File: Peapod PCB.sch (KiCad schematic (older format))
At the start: 16 parts, among them U1 ESP8266

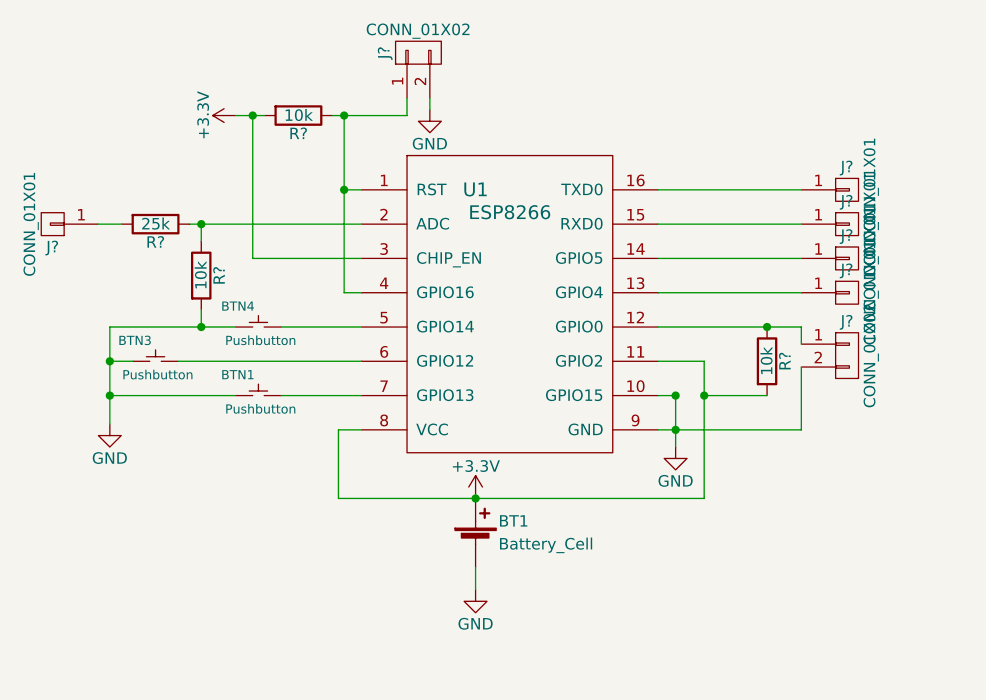
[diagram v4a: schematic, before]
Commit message: assigned footprints
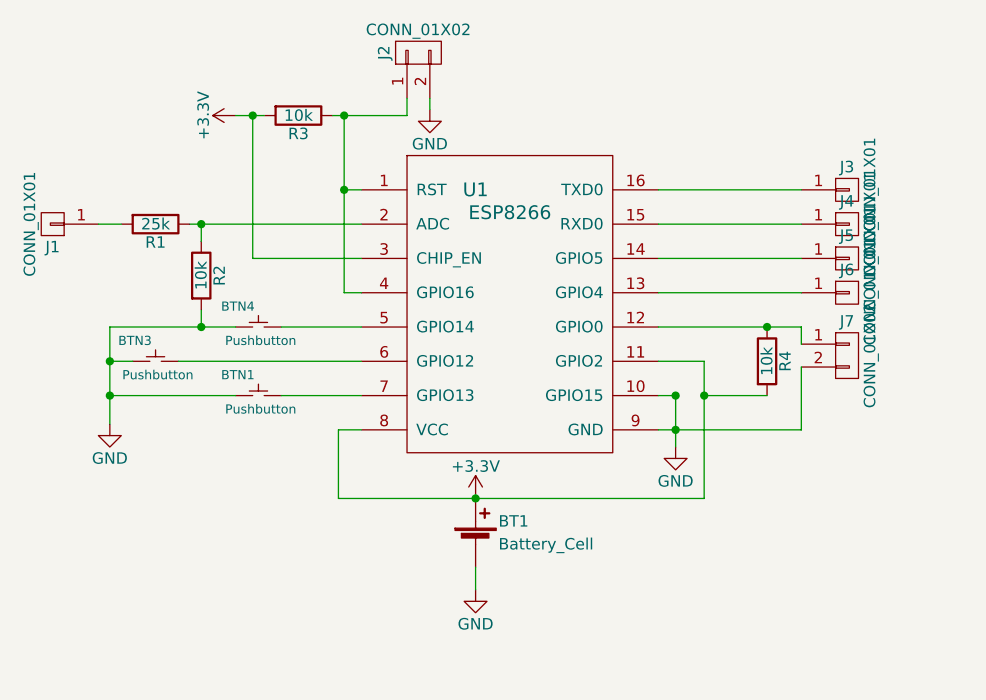
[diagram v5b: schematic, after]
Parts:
- BT1: footprint (none) -> mod:Battery Mount
- J1, J3, J4, J5, J6: renamed from J?; footprint (none) -> mod:Alligator Pad
- J2, J7: renamed from J?; footprint (none) -> mod:Bridge Pad
- R1, R2, R3, R4: renamed from R?; footprint (none) -> Resistors_SMD:R_0805_HandSoldering
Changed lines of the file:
@@
 F 0 "BT1" H 5925 4525 50  0000 L CNN
 F 1 "Battery_Cell" H 5925 4425 50  0000 L CNN
-F 2 "" V 5825 4485 50  0001 C CNN
+F 2 "mod:Battery Mount" V 5825 4485 50  0001 C CNN
 F 3 "" V 5825 4485 50  0001 C CNN
 	1    5825 4425
@@
 $EndComp
 $Comp
-L GND #PWR?
+L GND #PWR03
 U 1 1 5993357D
 P 4225 3900
-F 0 "#PWR?" H 4225 3650 50  0001 C CNN
+F 0 "#PWR03" H 4225 3650 50  0001 C CNN
 F 1 "GND" H 4225 3750 50  0000 C CNN
 F 2 "" H 4225 3900 50  0001 C CNN
@@
 $EndComp
 $Comp
-L CONN_01X01 J?
+L CONN_01X01 J3
 U 1 1 59933B2D
 P 7450 2875
-F 0 "J?" H 7450 2975 50  0000 C CNN
+F 0 "J3" H 7450 2975 50  0000 C CNN
 F 1 "CONN_01X01" V 7550 2875 50  0000 C CNN
-F 2 "" H 7450 2875 50  0001 C CNN
+F 2 "mod:Alligator Pad" H 7450 2875 50  0001 C CNN
 F 3 "" H 7450 2875 50  0001 C CNN
 	1    7450 2875
@@
 $EndComp
 $Comp
-L CONN_01X01 J?
+L CONN_01X01 J4
 U 1 1 59933BB9
 P 7450 3025
-F 0 "J?" H 7450 3125 50  0000 C CNN
+F 0 "J4" H 7450 3125 50  0000 C CNN
 F 1 "CONN_01X01" V 7550 3025 50  0000 C CNN
-F 2 "" H 7450 3025 50  0001 C CNN
+F 2 "mod:Alligator Pad" H 7450 3025 50  0001 C CNN
 F 3 "" H 7450 3025 50  0001 C CNN
 	1    7450 3025
@@
 $EndComp
 $Comp
-L CONN_01X01 J?
+L CONN_01X01 J5
 U 1 1 59933C1C
 P 7450 3175
-F 0 "J?" H 7450 3275 50  0000 C CNN
+F 0 "J5" H 7450 3275 50  0000 C CNN
 F 1 "CONN_01X01" V 7550 3175 50  0000 C CNN
-F 2 "" H 7450 3175 50  0001 C CNN
+F 2 "mod:Alligator Pad" H 7450 3175 50  0001 C CNN
 F 3 "" H 7450 3175 50  0001 C CNN
 	1    7450 3175
@@
 $EndComp
 $Comp
-L CONN_01X01 J?
+L CONN_01X01 J6
 U 1 1 59933C73
 P 7450 3325
-F 0 "J?" H 7450 3425 50  0000 C CNN
+F 0 "J6" H 7450 3425 50  0000 C CNN
 F 1 "CONN_01X01" V 7550 3325 50  0000 C CNN
-F 2 "" H 7450 3325 50  0001 C CNN
+F 2 "mod:Alligator Pad" H 7450 3325 50  0001 C CNN
 F 3 "" H 7450 3325 50  0001 C CNN
 	1    7450 3325
@@
 $EndComp
 $Comp
-L CONN_01X01 J?
+L CONN_01X01 J1
 U 1 1 59933CDE
 P 3975 3025
-F 0 "J?" H 3975 3125 50  0000 C CNN
+F 0 "J1" H 3975 3125 50  0000 C CNN
 F 1 "CONN_01X01" V 4075 3025 50  0000 C CNN
-F 2 "" H 3975 3025 50  0001 C CNN
+F 2 "mod:Alligator Pad" H 3975 3025 50  0001 C CNN
 F 3 "" H 3975 3025 50  0001 C CNN
 	1    3975 3025
@@
 $EndComp
 $Comp
-L R R?
+L R R3
 U 1 1 59933DD5
 P 5050 2550
-F 0 "R?" V 5130 2550 50  0000 C CNN
+F 0 "R3" V 5130 2550 50  0000 C CNN
 F 1 "10k" V 5050 2550 50  0000 C CNN
-F 2 "" V 4980 2550 50  0001 C CNN
+F 2 "Resistors_SMD:R_0805_HandSoldering" V 4980 2550 50  0001 C CNN
 F 3 "" H 5050 2550 50  0001 C CNN
 	1    5050 2550
@@
 $EndComp
 $Comp
-L +3.3V #PWR?
+L +3.3V #PWR04
 U 1 1 59933FE4
 P 4775 2550
-F 0 "#PWR?" H 4775 2400 50  0001 C CNN
+F 0 "#PWR04" H 4775 2400 50  0001 C CNN
 F 1 "+3.3V" H 4775 2690 50  0000 C CNN
 F 2 "" H 4775 2550 50  0001 C CNN
@@
 $EndComp
 $Comp
-L +3.3V #PWR?
+L +3.3V #PWR05
 U 1 1 59934256
 P 5825 4225
-F 0 "#PWR?" H 5825 4075 50  0001 C CNN
+F 0 "#PWR05" H 5825 4075 50  0001 C CNN
 F 1 "+3.3V" H 5825 4365 50  0000 C CNN
 F 2 "" H 5825 4225 50  0001 C CNN
@@
 $EndComp
 $Comp
-L R R?
+L R R1
 U 1 1 59934609
 P 4425 3025
-F 0 "R?" V 4505 3025 50  0000 C CNN
+F 0 "R1" V 4505 3025 50  0000 C CNN
 F 1 "25k" V 4425 3025 50  0000 C CNN
-F 2 "" V 4355 3025 50  0001 C CNN
+F 2 "Resistors_SMD:R_0805_HandSoldering" V 4355 3025 50  0001 C CNN
 F 3 "" H 4425 3025 50  0001 C CNN
 	1    4425 3025
@@
 	4275 3025 4175 3025
 $Comp
-L R R?
+L R R2
 U 1 1 59934849
 P 4625 3250
-F 0 "R?" V 4705 3250 50  0000 C CNN
+F 0 "R2" V 4705 3250 50  0000 C CNN
 F 1 "10k" V 4625 3250 50  0000 C CNN
-F 2 "" V 4555 3250 50  0001 C CNN
+F 2 "Resistors_SMD:R_0805_HandSoldering" V 4555 3250 50  0001 C CNN
 F 3 "" H 4625 3250 50  0001 C CNN
 	1    4625 3250
@@
 Connection ~ 4625 3475
 $Comp
-L CONN_01X02 J?
+L CONN_01X02 J7
 U 1 1 5993514F
 P 7450 3600
-F 0 "J?" H 7450 3750 50  0000 C CNN
+F 0 "J7" H 7450 3750 50  0000 C CNN
 F 1 "CONN_01X02" V 7550 3600 50  0000 C CNN
-F 2 "" H 7450 3600 50  0001 C CNN
+F 2 "mod:Bridge Pad" H 7450 3600 50  0001 C CNN
 F 3 "" H 7450 3600 50  0001 C CNN
 	1    7450 3600
@@
 Connection ~ 6700 3775
 $Comp
-L R R?
+L R R4
 U 1 1 59935339
 P 7100 3625
-F 0 "R?" V 7180 3625 50  0000 C CNN
+F 0 "R4" V 7180 3625 50  0000 C CNN
 F 1 "10k" V 7100 3625 50  0000 C CNN
-F 2 "" V 7030 3625 50  0001 C CNN
+F 2 "Resistors_SMD:R_0805_HandSoldering" V 7030 3625 50  0001 C CNN
 F 3 "" H 7100 3625 50  0001 C CNN
 	1    7100 3625
@@
 Connection ~ 6825 3775
 $Comp
-L CONN_01X02 J?
+L CONN_01X02 J2
 U 1 1 5993627D
 P 5575 2275
-F 0 "J?" H 5575 2425 50  0000 C CNN
+F 0 "J2" H 5575 2425 50  0000 C CNN
 F 1 "CONN_01X02" V 5675 2275 50  0000 C CNN
-F 2 "" H 5575 2275 50  0001 C CNN
+F 2 "mod:Bridge Pad" H 5575 2275 50  0001 C CNN
 F 3 "" H 5575 2275 50  0001 C CNN
 	1    5575 2275
@@
 Connection ~ 5250 2550
 $Comp
-L GND #PWR?
+L GND #PWR06
 U 1 1 599363AF
 P 5625 2525
-F 0 "#PWR?" H 5625 2275 50  0001 C CNN
+F 0 "#PWR06" H 5625 2275 50  0001 C CNN
 F 1 "GND" H 5625 2375 50  0000 C CNN
 F 2 "" H 5625 2525 50  0001 C CNN

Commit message: finished assigning footprints to components
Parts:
- BTN1, BTN3, BTN4: footprint (none) -> mod:Pushbutton
- U1: footprint (none) -> mod:ESP-12E_SMD
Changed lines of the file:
@@
 F 0 "U1" H 5825 3675 60  0000 C CNN
 F 1 "ESP8266" H 5975 3575 60  0000 C CNN
-F 2 "" H 5925 3275 60  0001 C CNN
+F 2 "mod:ESP-12E_SMD" H 5925 3275 60  0001 C CNN
 F 3 "" H 5925 3275 60  0001 C CNN
 	1    5925 3275
@@
 F 0 "BTN1" H 4785 3865 40  0000 C CNN
 F 1 "Pushbutton" H 4885 3715 40  0000 C CNN
-F 2 "" H 4575 3375 60  0001 C CNN
+F 2 "mod:Pushbutton" H 4575 3375 60  0001 C CNN
 F 3 "" H 4575 3375 60  0001 C CNN
 	1    4875 3775
@@
 F 0 "BTN3" H 4335 3715 40  0000 C CNN
 F 1 "Pushbutton" H 4435 3565 40  0000 C CNN
-F 2 "" H 4125 3225 60  0001 C CNN
+F 2 "mod:Pushbutton" H 4125 3225 60  0001 C CNN
 F 3 "" H 4125 3225 60  0001 C CNN
 	1    4425 3625
@@
 F 0 "BTN4" H 4785 3565 40  0000 C CNN
 F 1 "Pushbutton" H 4885 3415 40  0000 C CNN
-F 2 "" H 4575 3075 60  0001 C CNN
+F 2 "mod:Pushbutton" H 4575 3075 60  0001 C CNN
 F 3 "" H 4575 3075 60  0001 C CNN
 	1    4875 3475

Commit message: fixed changes
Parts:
- added R5: 10k, symbol R
- R3: footprint Resistors_SMD:R_0805_HandSoldering -> (none)
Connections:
- net +3V3: now also R3.1; no longer R3.2, U1.11 (GPIO2)
- net GND: now also R5.2; no longer U1.10 (GPIO15)
- net at J2.1 (P1), U1.1 (RST), U1.4 (GPIO16): no longer R3.1
- new net: R5.1, U1.10 (GPIO15)
- new net: R3.2, U1.11 (GPIO2)
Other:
- moved on the sheet: BT1, BTN1, BTN3, BTN4, J1, J2, R1, R2

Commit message: fixed battery mount
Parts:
- R3, R5: footprint (none) -> Resistors_SMD:R_0805_HandSoldering
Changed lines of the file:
@@
 $EndComp
 $Comp
-L GND #PWR5
+L GND #PWR01
 U 1 1 59932223
 P 4850 4225
-F 0 "#PWR5" H 4850 3975 50  0001 C CNN
+F 0 "#PWR01" H 4850 3975 50  0001 C CNN
 F 1 "GND" H 4850 4075 50  0000 C CNN
 F 2 "" H 4850 4225 50  0001 C CNN
@@
 $EndComp
 $Comp
-L GND #PWR6
+L GND #PWR02
 U 1 1 59932907
 P 6800 4100
-F 0 "#PWR6" H 6800 3850 50  0001 C CNN
+F 0 "#PWR02" H 6800 3850 50  0001 C CNN
 F 1 "GND" H 6800 3950 50  0000 C CNN
 F 2 "" H 6800 4100 50  0001 C CNN
@@
 $EndComp
 $Comp
-L GND #PWR1
+L GND #PWR03
 U 1 1 5993357D
 P 4500 3825
-F 0 "#PWR1" H 4500 3575 50  0001 C CNN
+F 0 "#PWR03" H 4500 3575 50  0001 C CNN
 F 1 "GND" H 4500 3675 50  0000 C CNN
 F 2 "" H 4500 3825 50  0001 C CNN
@@
 $EndComp
 $Comp
-L +3.3V #PWR2
+L +3.3V #PWR04
 U 1 1 59933FE4
 P 5300 3175
-F 0 "#PWR2" H 5300 3025 50  0001 C CNN
+F 0 "#PWR04" H 5300 3025 50  0001 C CNN
 F 1 "+3.3V" H 5300 3315 50  0000 C CNN
 F 2 "" H 5300 3175 50  0001 C CNN
@@
 $EndComp
 $Comp
-L +3.3V #PWR4
+L +3.3V #PWR05
 U 1 1 59934256
 P 4950 3925
-F 0 "#PWR4" H 4950 3775 50  0001 C CNN
+F 0 "#PWR05" H 4950 3775 50  0001 C CNN
 F 1 "+3.3V" H 4950 4065 50  0000 C CNN
 F 2 "" H 4950 3925 50  0001 C CNN
@@
 	4500 3775 5050 3775
 Wire Wire Line
-	4500 3475 4500 3625
-Wire Wire Line
-	4500 3625 4500 3775
-Wire Wire Line
-	4500 3775 4500 3825
+	4500 3475 4500 3825
 Connection ~ 4500 3625
 Wire Wire Line
@@
 	4950 4225 4850 4225
 Wire Wire Line
-	5125 2700 5125 2875
-Wire Wire Line
-	5125 2875 5125 3325
+	5125 2700 5125 3325
 Wire Wire Line
 	5125 2875 5325 2875
 Connection ~ 5125 2875
 Wire Wire Line
-	4825 3025 4875 3025
-Wire Wire Line
-	4875 3025 5325 3025
+	4825 3025 5325 3025
 $Comp
 L R R2
@@
 $EndComp
 Wire Wire Line
-	6625 3475 7100 3475
-Wire Wire Line
-	7100 3475 7250 3475
+	6625 3475 7250 3475
 Connection ~ 7100 3475
 $Comp
@@
 $EndComp
 $Comp
-L GND #PWR3
+L GND #PWR06
 U 1 1 599363AF
 P 5325 2700
-F 0 "#PWR3" H 5325 2450 50  0001 C CNN
+F 0 "#PWR06" H 5325 2450 50  0001 C CNN
 F 1 "GND" H 5325 2550 50  0000 C CNN
 F 2 "" H 5325 2700 50  0001 C CNN
@@
 $EndComp
 $Comp
-L +3.3V #PWR7
+L +3.3V #PWR07
 U 1 1 599466C8
 P 7100 3875
-F 0 "#PWR7" H 7100 3725 50  0001 C CNN
+F 0 "#PWR07" H 7100 3725 50  0001 C CNN
 F 1 "+3.3V" H 7100 4015 50  0000 C CNN
 F 2 "" H 7100 3875 50  0001 C CNN
@@
 F 0 "R3" V 6905 3625 50  0000 C CNN
 F 1 "10k" V 6825 3625 50  0000 C CNN
-F 2 "" V 6755 3625 50  0001 C CNN
+F 2 "Resistors_SMD:R_0805_HandSoldering" V 6755 3625 50  0001 C CNN
 F 3 "" H 6825 3625 50  0001 C CNN
 	1    6825 3625
@@
 F 0 "R5" V 6880 3925 50  0000 C CNN
 F 1 "10k" V 6800 3925 50  0000 C CNN
-F 2 "" V 6730 3925 50  0001 C CNN
+F 2 "Resistors_SMD:R_0805_HandSoldering" V 6730 3925 50  0001 C CNN
 F 3 "" H 6800 3925 50  0001 C CNN
 	1    6800 3925
@@
 	6625 3775 6800 3775
 $Comp
-L +3.3V #PWR?
+L +3.3V #PWR08
 U 1 1 59948486
 P 6975 3700
-F 0 "#PWR?" H 6975 3550 50  0001 C CNN
+F 0 "#PWR08" H 6975 3550 50  0001 C CNN
 F 1 "+3.3V" H 6975 3840 50  0000 C CNN
 F 2 "" H 6975 3700 50  0001 C CNN
@@
 	4875 2900 4875 3025
 $Comp
-L GND #PWR?
+L GND #PWR09
 U 1 1 5994872F
 P 4875 2525
-F 0 "#PWR?" H 4875 2275 50  0001 C CNN
+F 0 "#PWR09" H 4875 2275 50  0001 C CNN
 F 1 "GND" H 4875 2375 50  0000 C CNN
 F 2 "" H 4875 2525 50  0001 C CNN
@@
 	4875 2525 4875 2600
 $Comp
-L GND #PWR?
+L GND #PWR010
 U 1 1 599488CC
 P 7250 3750
-F 0 "#PWR?" H 7250 3500 50  0001 C CNN
+F 0 "#PWR010" H 7250 3500 50  0001 C CNN
 F 1 "GND" H 7250 3600 50  0000 C CNN
 F 2 "" H 7250 3750 50  0001 C CNN
@@
 $EndComp
 $Comp
-L GND #PWR?
+L GND #PWR011
 U 1 1 59948924
 P 6625 4000
-F 0 "#PWR?" H 6625 3750 50  0001 C CNN
+F 0 "#PWR011" H 6625 3750 50  0001 C CNN
 F 1 "GND" H 6625 3850 50  0000 C CNN
 F 2 "" H 6625 4000 50  0001 C CNN
